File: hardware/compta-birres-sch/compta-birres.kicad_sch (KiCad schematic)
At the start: 6 parts, among them P1 Conn_WallPlug_Earth, SW9 SW_Push, U1 ESP32-DevKitC

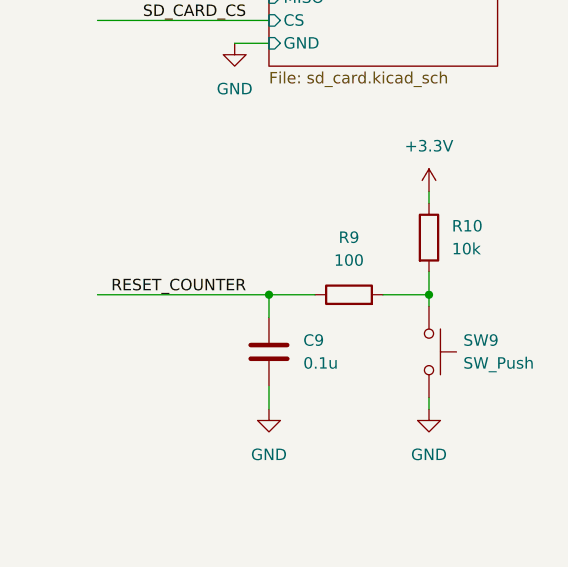
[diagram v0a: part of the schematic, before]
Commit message: Finalized buttons schematic, added tlp521-4
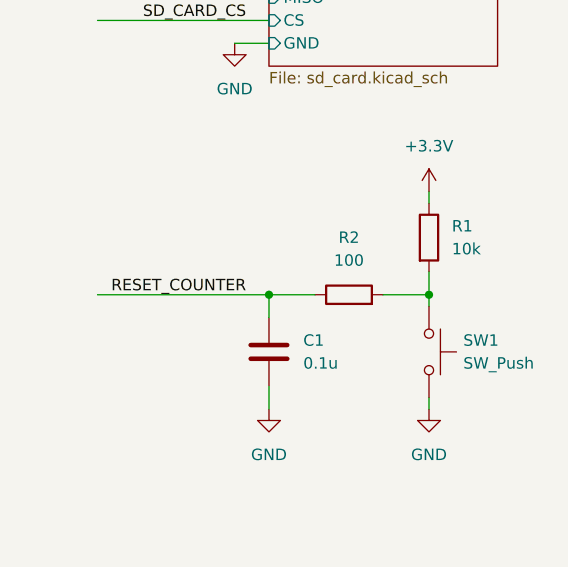
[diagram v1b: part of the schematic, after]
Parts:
- renumbered C9 to C1, R10 to R1, R9 to R2, SW9 to SW1
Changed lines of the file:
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@@
 	(title_block
 		(title "Root")
-		(date "2024-08-08")
-		(rev "1.3")
+		(date "2024-09-24")
+		(rev "1.4")
 		(company "Associació Cultural TGK")
 		(comment 1 "Author: lluc")
@@
 		(dnp no)
 		(fields_autoplaced yes)
-		(property "Reference" "#PWR051"
+		(property "Reference" "#PWR015"
 			(at 85.09 168.91 0)
 			(effects
@@
 			(project ""
 				(path "/9d879fd6-4f9b-4add-8486-efab784c3781"
-					(reference "#PWR051")
+					(reference "#PWR015")
 					(unit 1)
 				)
@@
 		(on_board yes)
 		(dnp no)
-		(property "Reference" "#PWR020"
+		(property "Reference" "#PWR010"
 			(at 224.79 118.11 0)
 			(effects
@@
 			(project "compta-birres"
 				(path "/9d879fd6-4f9b-4add-8486-efab784c3781"
-					(reference "#PWR020")
+					(reference "#PWR010")
 					(unit 1)
 				)
@@
 		(dnp no)
 		(fields_autoplaced yes)
-		(property "Reference" "#PWR02"
+		(property "Reference" "#PWR04"
 			(at 138.43 55.88 0)
 			(effects
@@
 			(project ""
 				(path "/9d879fd6-4f9b-4add-8486-efab784c3781"
-					(reference "#PWR02")
+					(reference "#PWR04")
 					(unit 1)
 				)
@@
 		(dnp no)
 		(fields_autoplaced yes)
-		(property "Reference" "#PWR07"
+		(property "Reference" "#PWR012"
 			(at 246.38 132.08 0)
 			(effects
@@
 			(project "compta-birres"
 				(path "/9d879fd6-4f9b-4add-8486-efab784c3781"
-					(reference "#PWR07")
+					(reference "#PWR012")
 					(unit 1)
 				)
@@
 		(dnp no)
 		(fields_autoplaced yes)
-		(property "Reference" "C9"
+		(property "Reference" "C1"
 			(at 232.41 144.7799 0)
 			(effects
@@
 			(project "compta-birres"
 				(path "/9d879fd6-4f9b-4add-8486-efab784c3781"
-					(reference "C9")
+					(reference "C1")
 					(unit 1)
 				)
@@
 		(dnp no)
 		(fields_autoplaced yes)
-		(property "Reference" "#PWR05"
+		(property "Reference" "#PWR07"
 			(at 220.98 68.58 0)
 			(effects
@@
 			(project "compta-birres"
 				(path "/9d879fd6-4f9b-4add-8486-efab784c3781"
-					(reference "#PWR05")
+					(reference "#PWR07")
 					(unit 1)
 				)
@@
 		(dnp no)
 		(fields_autoplaced yes)
-		(property "Reference" "#PWR021"
+		(property "Reference" "#PWR01"
 			(at 224.79 31.75 0)
 			(effects
@@
 			(project "compta-birres"
 				(path "/9d879fd6-4f9b-4add-8486-efab784c3781"
-					(reference "#PWR021")
+					(reference "#PWR01")
 					(unit 1)
 				)
@@
 		(on_board yes)
 		(dnp no)
-		(property "Reference" "#PWR08"
+		(property "Reference" "#PWR014"
 			(at 246.38 158.75 0)
 			(effects
@@
 			(project "compta-birres"
 				(path "/9d879fd6-4f9b-4add-8486-efab784c3781"
-					(reference "#PWR08")
+					(reference "#PWR014")
 					(unit 1)
 				)
@@
 		(on_board yes)
 		(dnp no)
-		(property "Reference" "#PWR022"
+		(property "Reference" "#PWR02"
 			(at 224.79 46.99 0)
 			(effects
@@
 			(project "compta-birres"
 				(path "/9d879fd6-4f9b-4add-8486-efab784c3781"
-					(reference "#PWR022")
+					(reference "#PWR02")
 					(unit 1)
 				)
@@
 		(dnp no)
 		(fields_autoplaced yes)
-		(property "Reference" "R9"
+		(property "Reference" "R2"
 			(at 237.49 133.35 90)
 			(effects
@@
 			(project "compta-birres"
 				(path "/9d879fd6-4f9b-4add-8486-efab784c3781"
-					(reference "R9")
+					(reference "R2")
 					(unit 1)
 				)
@@
 		(on_board yes)
 		(dnp no)
-		(property "Reference" "#PWR04"
+		(property "Reference" "#PWR08"
 			(at 224.79 90.17 0)
 			(effects
@@
 			(project "compta-birres"
 				(path "/9d879fd6-4f9b-4add-8486-efab784c3781"
-					(reference "#PWR04")
+					(reference "#PWR08")
 					(unit 1)
 				)
@@
 		(on_board yes)
 		(dnp no)
-		(property "Reference" "#PWR06"
+		(property "Reference" "#PWR013"
 			(at 228.6 158.75 0)
 			(effects
@@
 			(project "compta-birres"
 				(path "/9d879fd6-4f9b-4add-8486-efab784c3781"
-					(reference "#PWR06")
+					(reference "#PWR013")
 					(unit 1)
 				)
@@
 		(dnp no)
 		(fields_autoplaced yes)
-		(property "Reference" "#PWR052"
+		(property "Reference" "#PWR016"
 			(at 91.44 175.26 0)
 			(effects
@@
 			(project ""
 				(path "/9d879fd6-4f9b-4add-8486-efab784c3781"
-					(reference "#PWR052")
+					(reference "#PWR016")
 					(unit 1)
 				)
@@
 		(dnp no)
 		(fields_autoplaced yes)
-		(property "Reference" "#PWR053"
+		(property "Reference" "#PWR017"
 			(at 91.44 187.96 0)
 			(effects
@@
 			(project ""
 				(path "/9d879fd6-4f9b-4add-8486-efab784c3781"
-					(reference "#PWR053")
+					(reference "#PWR017")
 					(unit 1)
 				)
@@
 		(dnp no)
 		(fields_autoplaced yes)
-		(property "Reference" "#PWR049"
+		(property "Reference" "#PWR06"
 			(at 226.06 66.04 0)
 			(effects
@@
 			(project ""
 				(path "/9d879fd6-4f9b-4add-8486-efab784c3781"
-					(reference "#PWR049")
+					(reference "#PWR06")
 					(unit 1)
 				)
@@
 		(dnp no)
 		(fields_autoplaced yes)
-		(property "Reference" "R10"
+		(property "Reference" "R1"
 			(at 248.92 132.0799 0)
 			(effects
@@
 			(project "compta-birres"
 				(path "/9d879fd6-4f9b-4add-8486-efab784c3781"
-					(reference "R10")
+					(reference "R1")
 					(unit 1)
 				)
@@
 		(dnp no)
 		(fields_autoplaced yes)
-		(property "Reference" "#PWR01"
+		(property "Reference" "#PWR011"
 			(at 133.35 134.62 0)
 			(effects
@@
 			(project ""
 				(path "/9d879fd6-4f9b-4add-8486-efab784c3781"
-					(reference "#PWR01")
+					(reference "#PWR011")
 					(unit 1)
 				)
@@
 		(dnp no)
 		(fields_autoplaced yes)
-		(property "Reference" "#PWR09"
+		(property "Reference" "#PWR05"
 			(at 97.79 63.5 0)
 			(effects
@@
 			(project "compta-birres"
 				(path "/9d879fd6-4f9b-4add-8486-efab784c3781"
-					(reference "#PWR09")
+					(reference "#PWR05")
 					(unit 1)
 				)
@@
 		(dnp no)
 		(fields_autoplaced yes)
-		(property "Reference" "SW9"
+		(property "Reference" "SW1"
 			(at 250.19 144.7799 90)
 			(effects
@@
 			(project "compta-birres"
 				(path "/9d879fd6-4f9b-4add-8486-efab784c3781"
-					(reference "SW9")
+					(reference "SW1")
 					(unit 1)
 				)
@@
 		(dnp no)
 		(fields_autoplaced yes)
-		(property "Reference" "#PWR017"
+		(property "Reference" "#PWR09"
 			(at 224.79 102.87 0)
 			(effects
@@
 			(project "compta-birres"
 				(path "/9d879fd6-4f9b-4add-8486-efab784c3781"
-					(reference "#PWR017")
+					(reference "#PWR09")
 					(unit 1)
 				)

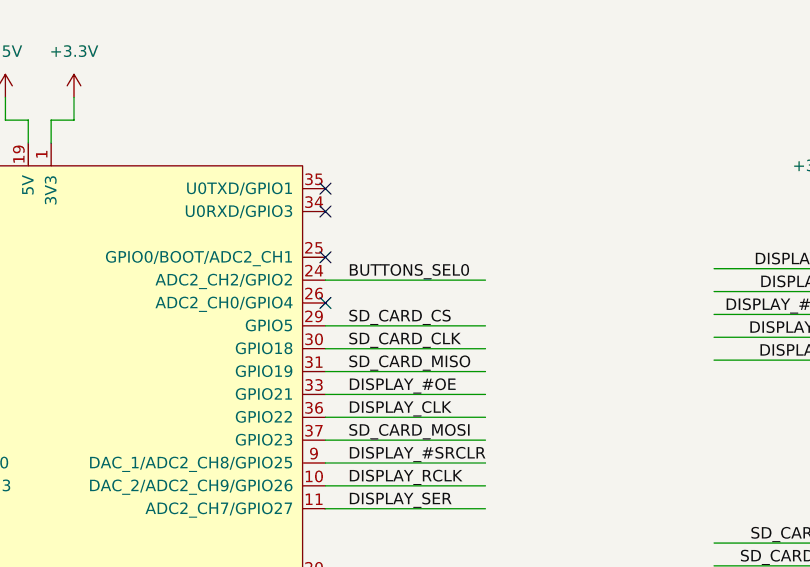
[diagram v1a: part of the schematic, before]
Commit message: Changed SEL0 pin from 2 to 4
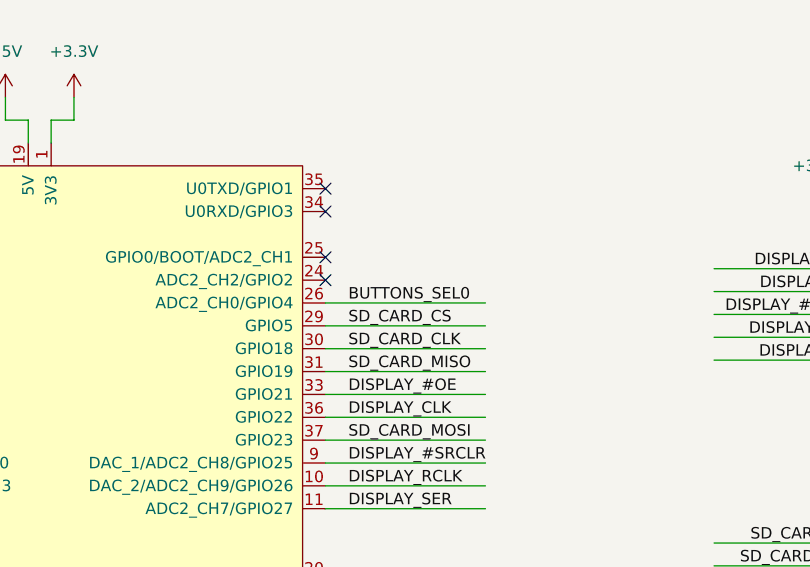
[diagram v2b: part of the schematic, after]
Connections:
- net BUTTONS_SEL0: now also U1.26 (ADC2_CH0/GPIO4); no longer U1.24 (ADC2_CH2/GPIO2)
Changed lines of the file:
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@@
 	(title_block
 		(title "Root")
-		(date "2024-09-24")
-		(rev "1.4")
+		(date "2024-09-27")
+		(rev "1.5")
 		(company "Associació Cultural TGK")
 		(comment 1 "Author: lluc")
@@
 	)
 	(no_connect
-		(at 166.37 74.93)
+		(at 166.37 72.39)
 	)
 	(no_connect
@@
 	(wire
 		(pts
-			(xy 166.37 72.39) (xy 184.15 72.39)
+			(xy 166.37 74.93) (xy 184.15 74.93)
 		)
 		(stroke
@@
 		)
 	)
+	(label "BUTTONS_SEL0"
+		(at 168.91 74.93 0)
+		(fields_autoplaced yes)
+		(effects
+			(font
+				(size 1.27 1.27)
+			)
+			(justify left bottom)
+		)
+	)
 	(label "SD_CARD_MOSI"
 		(at 168.91 90.17 0)
@@
 		)
 	)
-	(label "BUTTONS_SEL0"
-		(at 168.91 72.39 0)
-		(fields_autoplaced yes)
-		(effects
-			(font
-				(size 1.27 1.27)
-			)
-			(justify left bottom)
-		)
-	)

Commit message: final?¿ schematic update
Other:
- sheet Buttons ports: added 12V; removed none
